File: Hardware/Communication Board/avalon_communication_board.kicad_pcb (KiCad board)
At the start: 2 copper layers, 126 x 70 mm, 110 parts, among them IC1 ENC28J60-I/SO, J1 RJ45_LEDS, P1 MC34629, P10 8 Pin SIL, P11 8 Pin SIL, P12 2x3 Pin SIL, P13 MC34631, P14 MC34631, P15 MC34631, P16 MC34631, P17 MC34631, P18 MC34631, P19 Power Board Connector, P2 MC34633, P3 MC34633, P4 MC34633, P5 MC34633, P6 6 Pin SIL, P7 10 Pin SIL, P8 8 Pin SIL, P9 8 Pin SIL, Q1 FMMT597, Q2 BC817, Q3 BC817, Q4 FMMT597, Q5 BC817, SW1 B3U-1000P, SW2 B3U-1000P, U1 B78476A8247A003, U2 MPU9250, U3 LM2575S, U4 ESP-12S, U5 LM2776, U6 BH76330FVM, U7 BH76330FVM, U8 LMH6643, U9 LMH6643, Y1 ABM3-25MHz

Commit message: -Locked arduino header footprints to ensure they are not moved from their precise locations -Removed all footprints from board area to begin more optimal routing session
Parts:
- moved SW2 400.4 mm to (287.4, 98.6)
- moved R3 398.4 mm to (294.2, 79.7), turned to 270 degrees
- moved R1 390.2 mm to (288.1, 92.5), turned to 270 degrees
- moved R5 389.0 mm to (288.4, 79.7), turned to 90 degrees
- moved R17 376.9 mm to (267.4, 103.3)
- moved P1 360.5 mm to (298.4, 63.2)
- moved R16 356.5 mm to (281.7, 90.8), turned to 180 degrees
- moved P3 355.1 mm to (250.3, 85.8), turned to 90 degrees
- moved R20 344.6 mm to (267.2, 122.3)
- moved C13 341.9 mm to (274.2, 98.6), turned to 270 degrees
- moved Q2 333.2 mm to (292.3, 73.6), turned to 270 degrees
- moved R6 328.2 mm to (298.8, 72.7), turned to 270 degrees
- moved Q1 328.0 mm to (274.7, 91.5), turned to 90 degrees
- moved U6 327.5 mm to (261.7, 115.8)
- moved C21 322.8 mm to (273.0, 128.3), turned to 180 degrees
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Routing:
- removed copper zone on B.Cu, net GND
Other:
- board size 126 x 70 mm -> 104 x 70 mm

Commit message: -Layout and Routing complete for communication board -Silk Screen of board needs changing in order to produce a readable output -Design Rules file created -Footprint for MPU9250 created
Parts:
- removed SW2: B3U-1000P, kicad-open-modules-master:B3U-1000P
- added D3: LED, Diodes_SMD:D_1206, F.Cu at (107.6, 127.3)
- added D4: LED, Diodes_SMD:D_1206, F.Cu at (128.9, 62.6)
- added R34: 100R, Resistors_SMD:R_1206_HandSoldering, F.Cu at (112.4, 127.7)
- added R35: 220R, Resistors_SMD:R_1206_HandSoldering, F.Cu at (133.6, 61.5)
- added R36: 100K, Resistors_SMD:R_1206_HandSoldering, B.Cu at (201.5, 115.2)
- C26, C27: footprint Communication Board Footprints:EEEFK1E471P -> Capacitors_SMD:C_1206_HandSoldering
- Q1, Q2, Q3, Q4, Q5, R1, R17, R2, R3, R4, R5, R6: moved to B.Cu
- U2: footprint Socket_Strips:Socket_Strip_Straight_1x04_Pitch2.54mm -> Communication Board Footprints:MPU9250
- moved R7 196.6 mm to (156.8, 67.7), turned to 0 degrees
- moved R8 195.2 mm to (163.5, 67.7), turned to 180 degrees
- moved C3 193.4 mm to (144.6, 88.2), turned to 270 degrees
- moved C11 186.3 mm to (174.0, 64.5)
- moved C2 185.6 mm to (110.9, 120.4)
- moved C8 183.4 mm to (171.7, 76.4), turned to 180 degrees
- moved C12 179.1 mm to (169.0, 64.5)
- moved C5 178.0 mm to (176.5, 64.5)
- moved D2 174.4 mm to (120.5, 75.8), turned to 180 degrees
- moved C4 172.5 mm to (147.2, 88.2), turned to 270 degrees
- moved D1 171.9 mm to (126.5, 114.4), turned to 90 degrees
- moved C7 171.6 mm to (173.2, 84.6), turned to 270 degrees
- moved IC1 170.9 mm to (159.4, 82.0), turned to 90 degrees
- moved C14 169.4 mm to (111.2, 80.8), turned to 0 degrees
- moved R11 167.9 mm to (166.3, 73.8), turned to 0 degrees
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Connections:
- U4 pad 10: Net-(SW2-Pad2) -> Net-(R36-Pad1)
- U4 pad 12: Net-(SW2-Pad2) -> Net-(R17-Pad2)
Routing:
- net +3V3: track 0.00 -> 355.3 mm, vias 0 -> 6
- net +5V: track 0.00 -> 310.0 mm, vias 0 -> 4
- net +12V: track 0.00 -> 210.1 mm, vias 0 -> 8
- net GND: track 0.00 -> 123.8 mm, vias 0 -> 56
- net GPIO_57: track 0.00 -> 75.0 mm, vias 0 -> 5
- net LEDA: track 0.00 -> 74.3 mm, vias 0 -> 1
- net Net-(R18-Pad2): track 0.00 -> 70.6 mm
- net ESP_SDA: track 0.00 -> 67.5 mm
- net LEDB: track 0.00 -> 66.6 mm, vias 0 -> 3
- net GPIO_55: track 0.00 -> 63.1 mm
- net GPIO_56: track 0.00 -> 61.9 mm
- net GPIO_59: track 0.00 -> 60.5 mm, vias 0 -> 2
- net ESP_SCL: track 0.00 -> 56.1 mm
- net GPIO_58: track 0.00 -> 55.2 mm, vias 0 -> 3
- net Net-(R17-Pad2): track 0.00 -> 54.8 mm, vias 0 -> 1
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- added copper zone on B.Cu, net GND
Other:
- board size 104 x 70 mm -> 101 x 70 mm
- net class Power added: clearance 0.2, trace_width 0.4, via_dia 0.6, via_drill 0.4

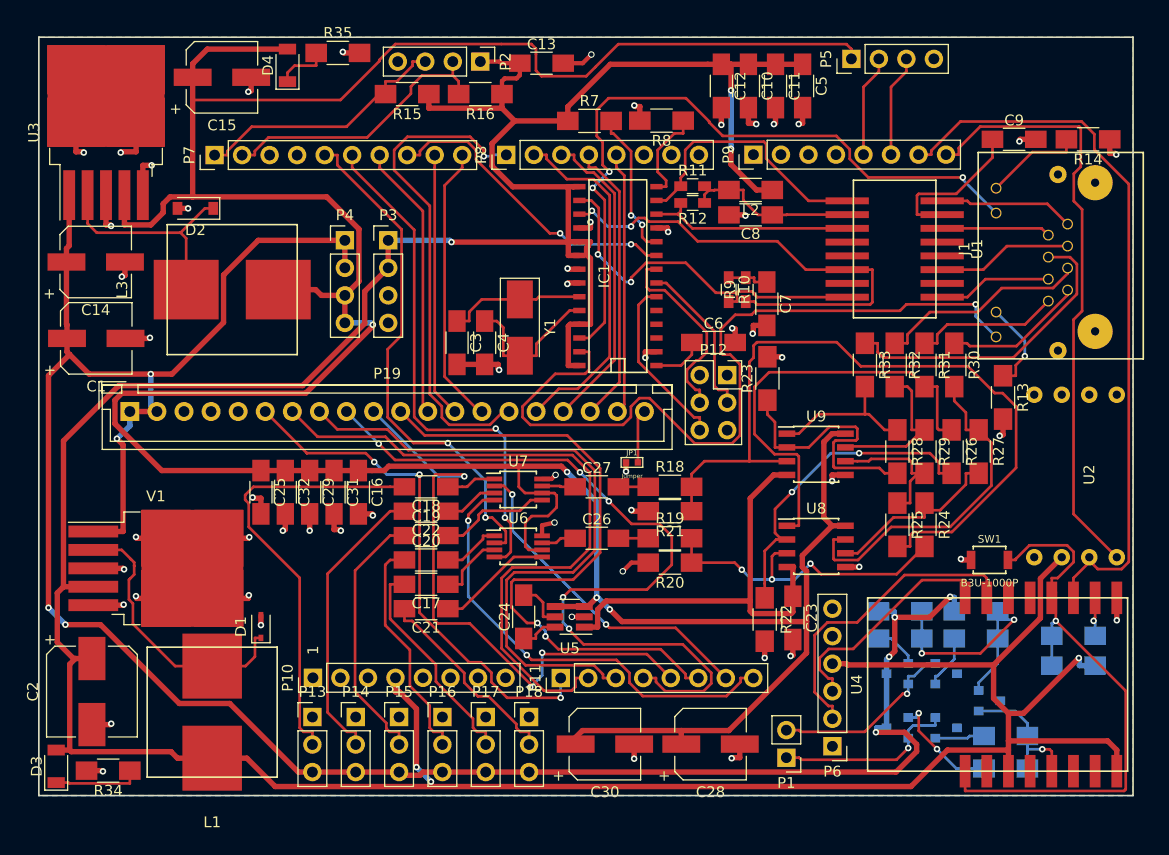
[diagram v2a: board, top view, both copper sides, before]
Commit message: -Completed circuit board autorouting -Generated test Gerber files to check pricing of circuit board -Significantly reduced layout size through component placement optimization
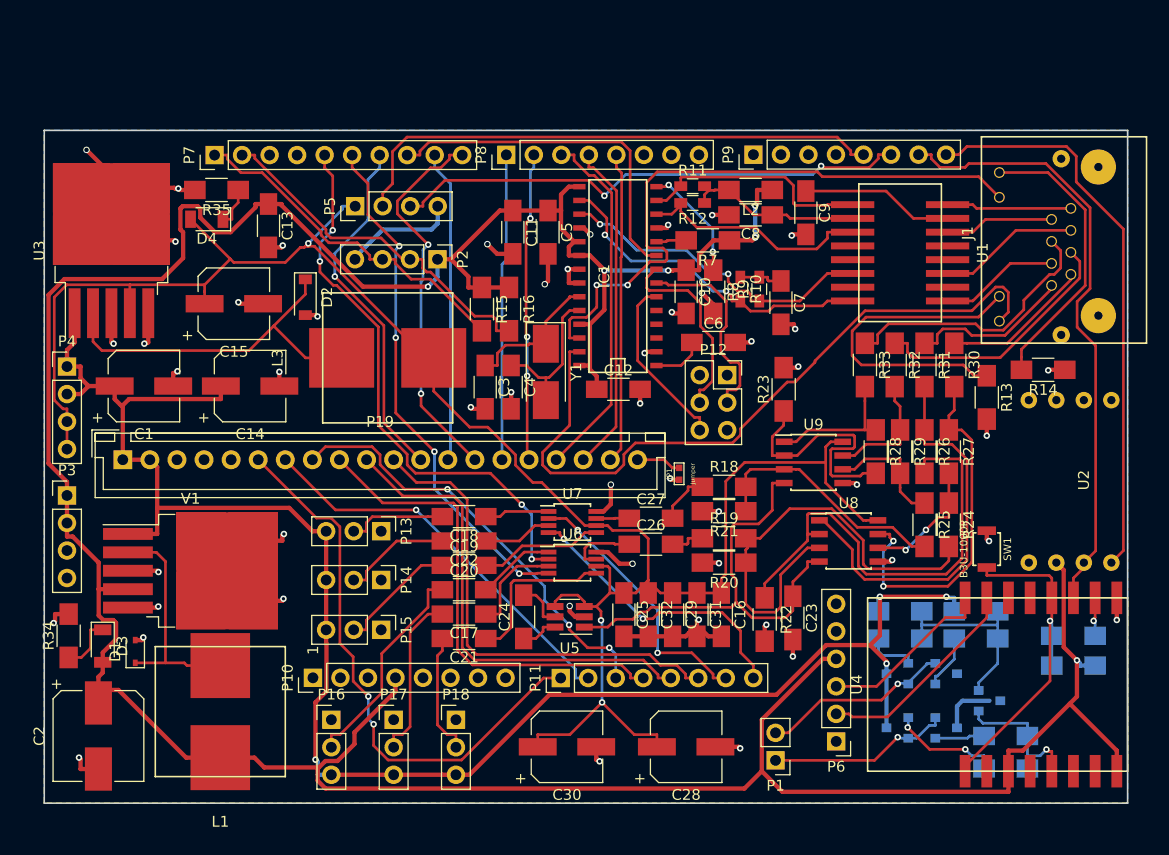
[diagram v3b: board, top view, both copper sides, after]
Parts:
- moved P5 47.8 mm to (135.2, 75.6)
- moved P3 37.9 mm to (108.6, 102.3)
- moved C16 35.4 mm to (169.0, 113.3)
- moved C25 35.4 mm to (160.0, 113.3)
- moved C29 35.4 mm to (164.5, 113.3)
- moved C31 35.4 mm to (166.8, 113.3)
- moved C32 35.4 mm to (162.2, 113.3)
- moved C12 29.6 mm to (159.5, 92.5), turned to 0 degrees
- moved C13 29.3 mm to (127.2, 77.4), turned to 270 degrees
- moved P4 28.2 mm to (108.6, 90.4)
- moved C11 27.8 mm to (149.8, 78.0)
- moved C5 27.1 mm to (153.0, 78.0)
- moved R14 21.7 mm to (198.7, 90.7)
- moved R15 21.0 mm to (146.9, 85.1), turned to 270 degrees
- moved C15 20.9 mm to (124.0, 84.6)
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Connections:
- P2 pad 4: Net-(P2-Pad4) -> GND
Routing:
- net +5V: track 310.0 -> 184.2 mm, vias 4 -> 3
- net +12V: track 210.1 -> 161.4 mm, vias 8 -> 4
- net Net-(R18-Pad2): track 70.6 -> 23.1 mm
- net BLUE_RX: track 9.43 -> 50.3 mm
- net +3V3: track 355.3 -> 314.6 mm
- net BLUE_TX: track 9.43 -> 48.1 mm, vias 0 -> 2
- net Net-(C18-Pad2): track 41.1 -> 9.22 mm
- net GPIO_57: track 75.0 -> 44.3 mm, vias 5 -> 0
- net GND: track 123.8 -> 153.3 mm, vias 56 -> 50
- net GPIO_55: track 63.1 -> 36.8 mm, vias 0 -> 1
- net Net-(R17-Pad2): track 54.8 -> 32.2 mm
- net Net-(J1-Pad11): track 8.50 -> 30.4 mm, vias 1 -> 0
- net GPIO_56: track 61.9 -> 40.2 mm, vias 0 -> 3
- net Net-(J1-Pad9): track 9.05 -> 26.6 mm
- net POW_PWM_2: track 45.5 -> 28.3 mm, vias 1 -> 0
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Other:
- board size 101 x 70 mm -> 100 x 62.1 mm

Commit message: -Updated PCB layout to ensure decoupling capacitors are close to IC's -Re routed Arduino Due SPI connector to ensure pinout is correct
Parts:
- moved C31 21.7 mm to (177.9, 94.7), turned to 0 degrees
- moved C16 19.1 mm to (186.4, 105.5)
- moved C29 9.79 mm to (154.9, 111.4), turned to 0 degrees
- moved C32 7.32 mm to (159.8, 106.4), turned to 90 degrees
- moved SW1 4.63 mm to (196.7, 103.9)
- moved R24 1.80 mm to (191.8, 105.0)
- moved C26 1.75 mm to (164.2, 106.4)
- moved C27 1.71 mm to (164.2, 104.2)
- moved R23 1.65 mm to (173.1, 92.4)
- moved R20 1.58 mm to (170.8, 108.8)
- moved R21 1.56 mm to (170.8, 103.9)
- moved R19 1.55 mm to (170.8, 106.2)
- moved R25 1.35 mm to (189.1, 105.0)
- moved U5 1.20 mm to (155.0, 114.7)
- moved R18 1.15 mm to (170.4, 101.6)
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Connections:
- P12 pad 2: Net-(P12-Pad2) -> Ether_SO
- P12 pad 6: Ether_SO -> Net-(P12-Pad6)
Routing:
- net +5V: track 184.2 -> 198.2 mm, vias 3 -> 6
- net GND: track 153.3 -> 162.3 mm, vias 50 -> 53
- net Net-(R19-Pad2): track 42.6 -> 50.6 mm, vias 0 -> 3
- net Net-(R22-Pad1): track 42.8 -> 48.0 mm
- net Net-(R26-Pad1): track 36.7 -> 41.2 mm
- net Net-(R27-Pad1): track 33.5 -> 37.2 mm
- net Net-(R24-Pad1): track 12.0 -> 15.4 mm
- net Net-(C27-Pad1): track 3.06 -> 6.45 mm
- net Ether_SO: track 16.2 -> 13.8 mm
- net Net-(R18-Pad2): track 23.1 -> 25.1 mm
- net Ether_SI: track 18.8 -> 20.7 mm
- net Net-(R25-Pad1): track 11.4 -> 13.1 mm
- net LEDA: track 67.0 -> 68.5 mm
- net Net-(C27-Pad2): track 4.82 -> 3.51 mm
- net -5V: track 42.4 -> 43.4 mm
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
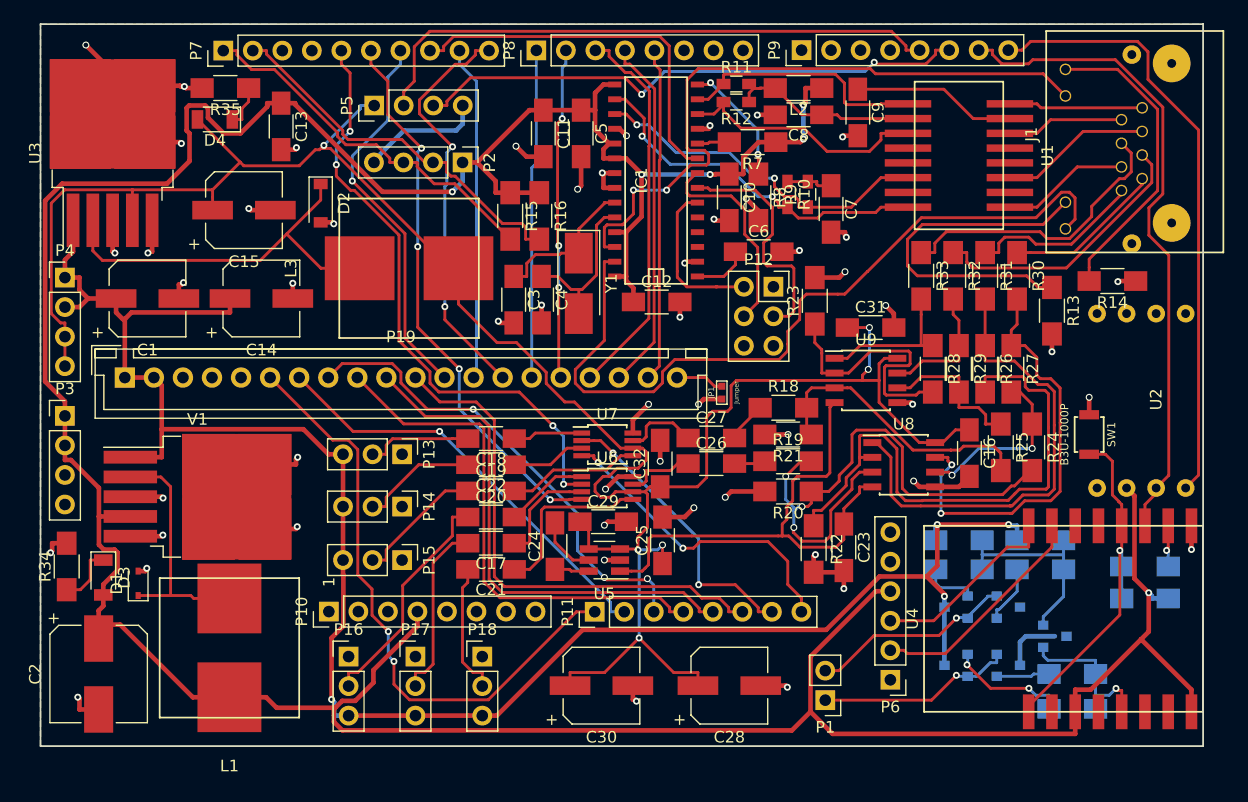
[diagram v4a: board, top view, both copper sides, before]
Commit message: -Moved capacitors for camera switching and transmission section to ensure decoupling operates correctly -Communication Board PCB Routing and Design Complete -Silk Screen of Communication Board modified to ensure component labels are clear -Gerber files updated to include new design
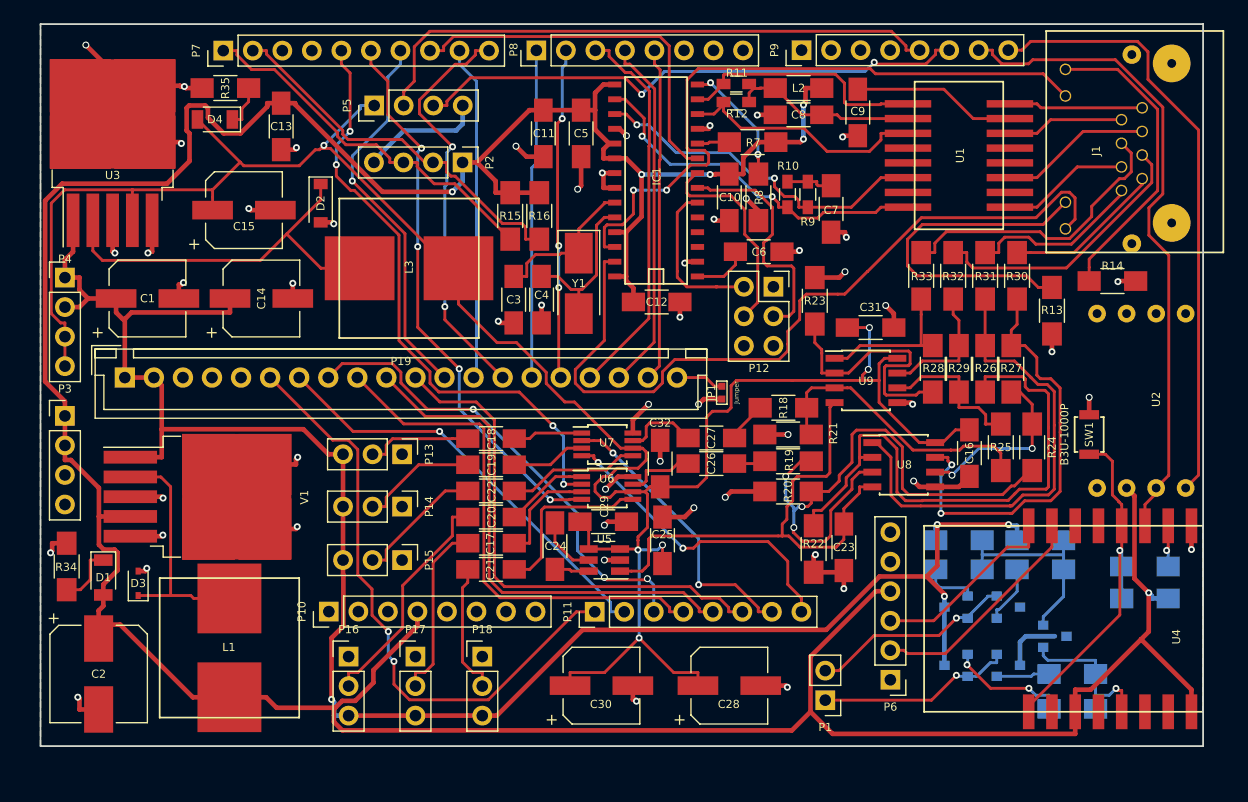
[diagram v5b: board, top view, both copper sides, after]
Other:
- board text removed: "1"

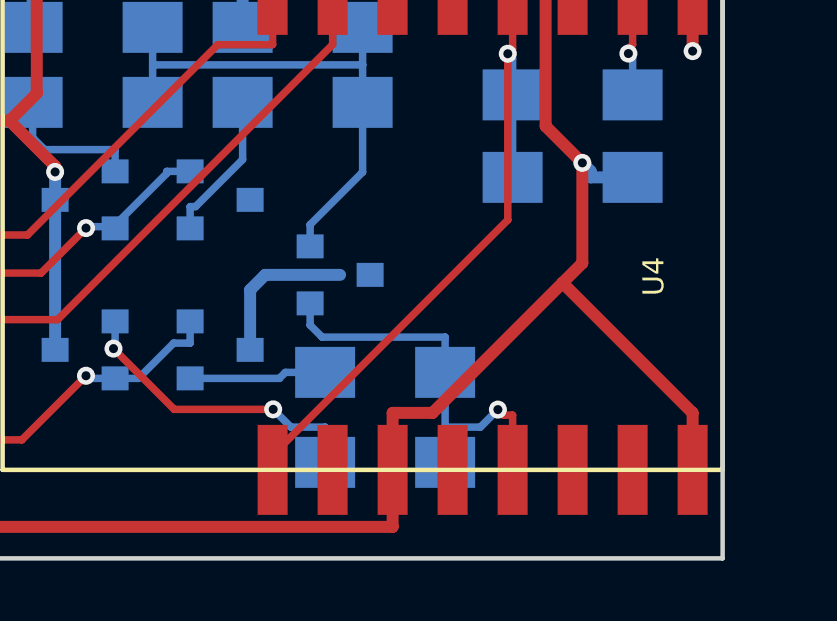
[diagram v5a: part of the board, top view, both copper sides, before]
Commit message: -Fixed issue in ultrasonic transducer transmitter circuitry where transistor did not have base current limiting resistor -Updated PCB to account of additional resistor for ultrasonic transducer circuitry -Updated gerber files to reflect new pcb design
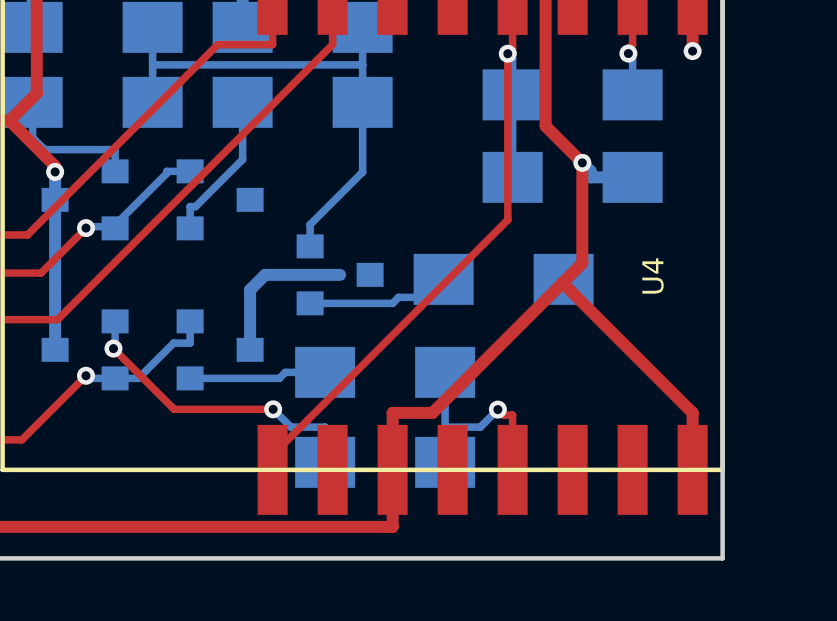
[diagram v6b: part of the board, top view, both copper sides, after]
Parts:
- added R37: 1.5K, Resistors_SMD:R_1206_HandSoldering, B.Cu at (199.2, 121.4)
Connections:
- Q5 pad 1: ULTRA_CTRL -> Net-(Q5-Pad1)
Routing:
- net Net-(Q5-Pad1): track 0.00 -> 4.78 mm
- net ULTRA_CTRL: track 14.0 -> 12.6 mm

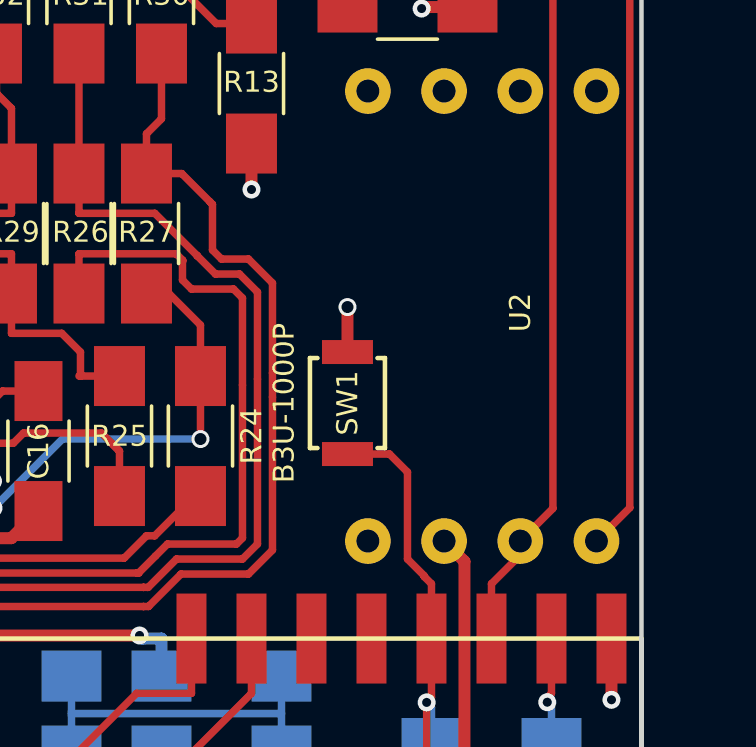
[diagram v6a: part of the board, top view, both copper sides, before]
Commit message: -Added the Avalon Logo to the Communication Board PCB -Added the Avalon Logo Footprint File -Added the Avalon Logo to the Communication Board Schematic -Added the release mechanism circuit board files and design to the repository -Updated Communication Board Gerber Files
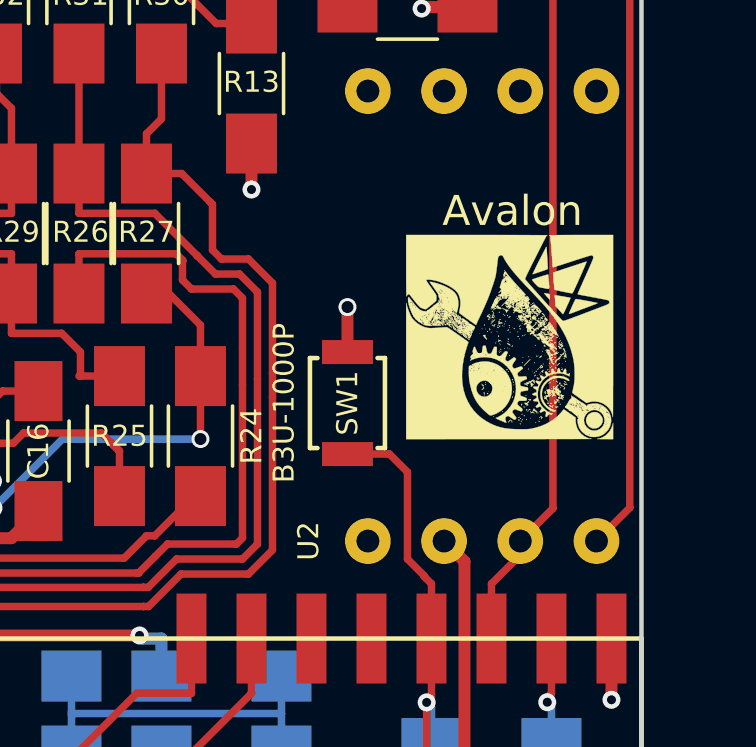
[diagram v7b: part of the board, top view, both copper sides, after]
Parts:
- added G***: LOGO, Footprints:Avalon Logo Footprint, F.Cu at (202.1, 101.7)
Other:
- board text added: "Avalon"
